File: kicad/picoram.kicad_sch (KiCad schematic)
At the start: 11 parts, among them U1 Pico, U2 4164, U3 TXS0108EPW, U4 41256, U5 74HCT244

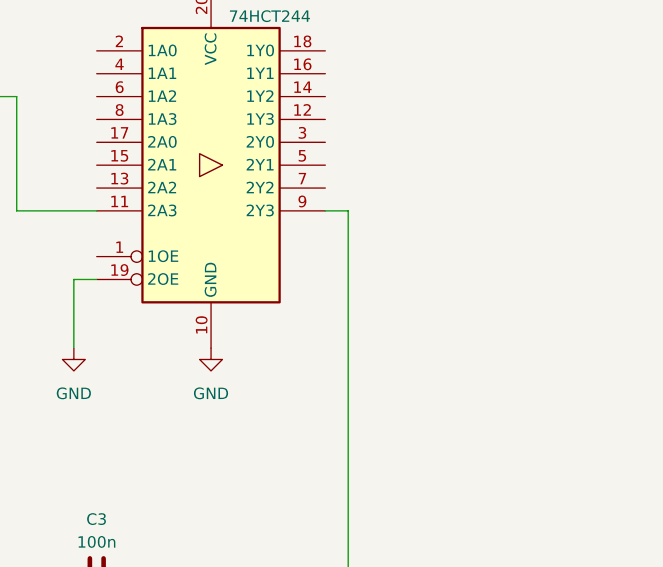
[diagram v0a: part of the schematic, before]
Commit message: add additional pulldown to buffer input
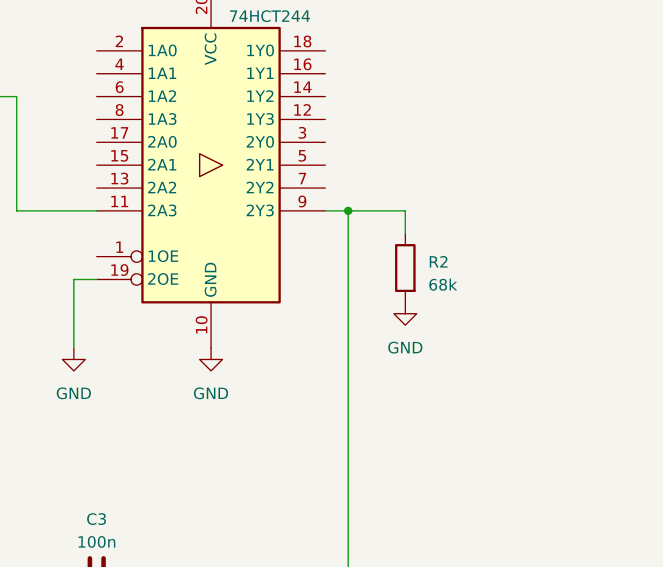
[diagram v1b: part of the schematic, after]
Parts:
- added R2: 68k, symbol Device:R
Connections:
- net GND: now also R2.2
- net at U4.14 (DOUT), U5.9 (2Y3): now also R2.1
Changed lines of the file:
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@@
   (junction (at 148.59 50.8) (diameter 0) (color 0 0 0 0)
   )
+  (junction (at 233.68 66.04) (diameter 0) (color 0 0 0 0)
+  )
   (junction (at 120.65 69.85) (diameter 0) (color 0 0 0 0)
   )
@@
     (stroke (width 0) (type default))
   )
+  (wire (pts (xy 240.03 66.04) (xy 240.03 68.58))
+    (stroke (width 0) (type default))
+  )
   (wire (pts (xy 176.53 86.36) (xy 176.53 78.74))
     (stroke (width 0) (type default))
@@
     (stroke (width 0) (type default))
   )
+  (wire (pts (xy 233.68 66.04) (xy 233.68 124.46))
+    (stroke (width 0) (type default))
+  )
   (wire (pts (xy 77.47 102.87) (xy 72.39 102.87))
     (stroke (width 0) (type default))
@@
     (stroke (width 0) (type default))
   )
-  (wire (pts (xy 233.68 66.04) (xy 233.68 124.46))
+  (wire (pts (xy 233.68 66.04) (xy 240.03 66.04))
     (stroke (width 0) (type default))
   )
@@
         (path "/22b3f9c4-9e40-4992-9a15-57379e658900"
           (reference "#PWR010") (unit 1)
+        )
+      )
+    )
+  )
+  (symbol (lib_id "power:GND") (at 240.03 76.2 0) (mirror y) (unit 1)
+    (in_bom yes) (on_board yes) (dnp no) (fields_autoplaced)
+    (property "Reference" "#PWR019" (at 240.03 82.55 0)
+      (effects (font (size 1.27 1.27)) hide)
+    )
+    (property "Value" "GND" (at 240.03 81.28 0)
+      (effects (font (size 1.27 1.27)))
+    )
+    (property "Footprint" "" (at 240.03 76.2 0)
+      (effects (font (size 1.27 1.27)) hide)
+    )
+    (property "Datasheet" "" (at 240.03 76.2 0)
+      (effects (font (size 1.27 1.27)) hide)
+    )
+    (pin "1")
+    (instances
+      (project "picoram"
+        (path "/22b3f9c4-9e40-4992-9a15-57379e658900"
+          (reference "#PWR019") (unit 1)
         )
       )
@@
         )
       )
+    )
+  )
+  (symbol (lib_id "Device:R") (at 240.03 72.39 0) (mirror y) (unit 1)
+    (in_bom yes) (on_board yes) (dnp no) (fields_autoplaced)
+    (property "Reference" "R2" (at 242.57 71.755 0)
+      (effects (font (size 1.27 1.27)) (justify right))
+    )
+    (property "Value" "68k" (at 242.57 74.295 0)
+      (effects (font (size 1.27 1.27)) (justify right))
+    )
+    (property "Footprint" "" (at 241.808 72.39 90)
+      (effects (font (size 1.27 1.27)) hide)
+    )
+    (property "Datasheet" "~" (at 240.03 72.39 0)
+      (effects (font (size 1.27 1.27)) hide)
+    )
+    (pin "1")
+    (pin "2")
+    (instances
+      (project "picoram"
+        (path "/22b3f9c4-9e40-4992-9a15-57379e658900"
+          (reference "R2") (unit 1)
+        )
+      )
